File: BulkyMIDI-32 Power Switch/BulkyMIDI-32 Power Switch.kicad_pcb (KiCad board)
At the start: 2 copper layers, 100 x 100 mm, 57 parts, among them J1 DC IN, J2 CH2, J3 CH1, J4 CH3, J5 CH4, J6 Power Panel, J7 CH5, K1 HK19F-DC, K2 HK19F-DC, K3 HK19F-DC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

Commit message: Fixes panel errors and inconsistencies
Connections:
- D2 pad 1: GND -> PWR
- D2 pad 2: PWR -> +5V
- D3 pad 1: GND -> SYS
- D3 pad 2: SYS -> +5V
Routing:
- net +5V: track 204.6 -> 271.3 mm
- net PWR: track 37.6 -> 39.7 mm
- net SYS: track 47.2 -> 49.2 mm
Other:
- board text added: "BulkyMIDI-32 Power Switch (rev. B) github.com/tebl"
- board text removed: "BulkyMIDI-32 Power Switch (rev. A) github.com/tebl"

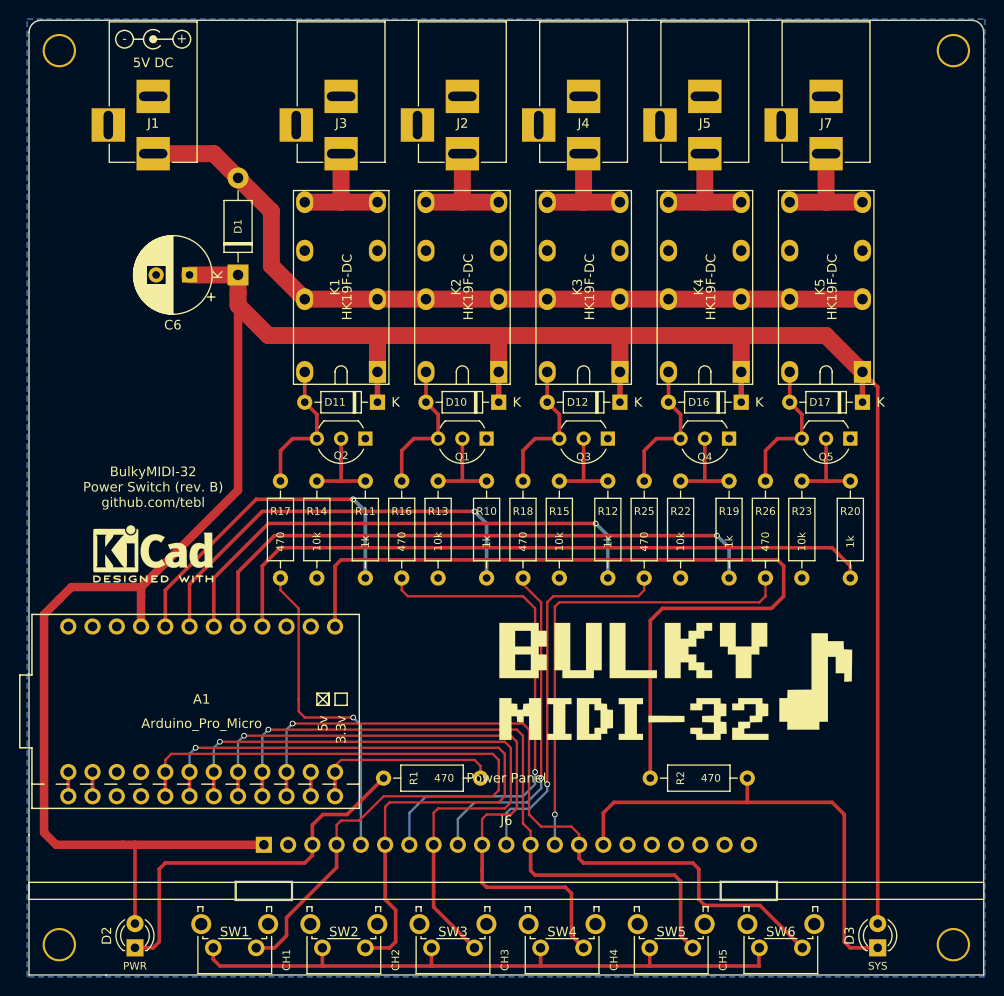
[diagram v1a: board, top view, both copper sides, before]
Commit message: Updated Power Switch to incorporate changes
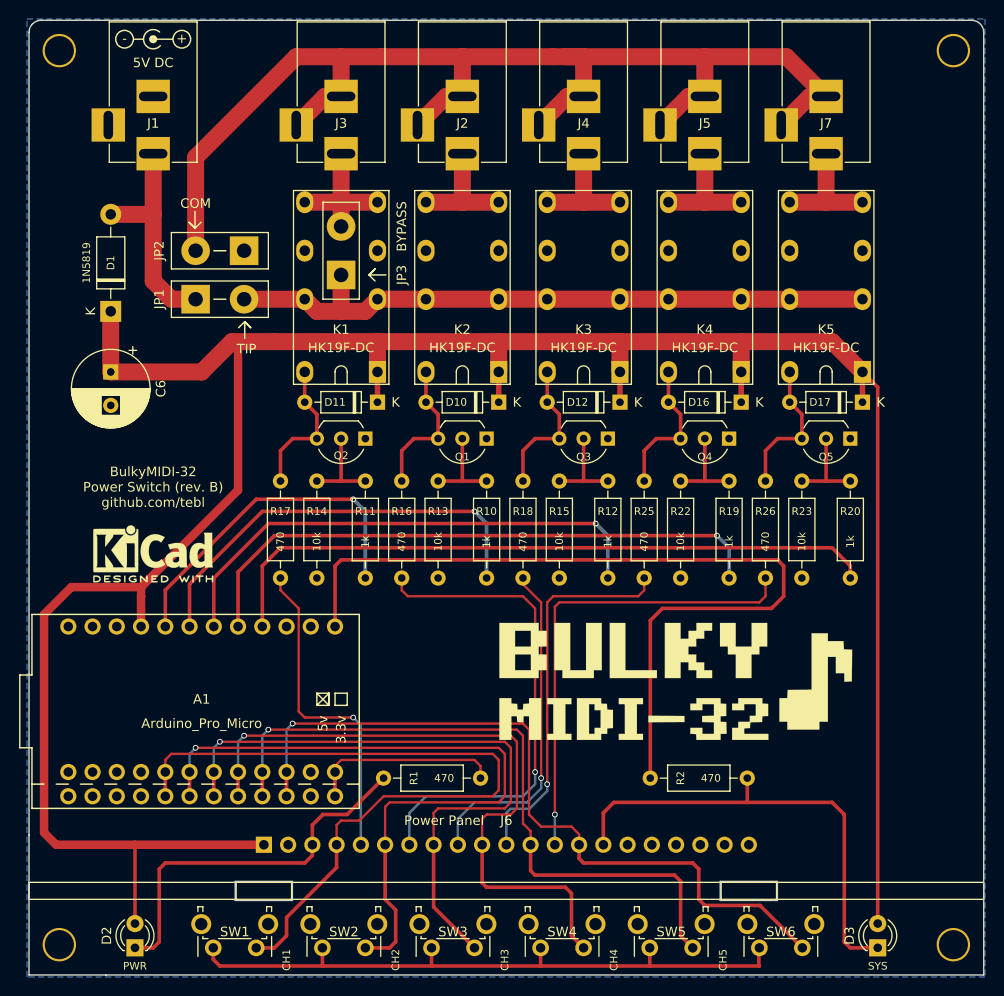
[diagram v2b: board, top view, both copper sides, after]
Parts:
- added JP1: TIP, wire_pads:WireLink, F.Cu at (87.6, 83.8)
- added JP2: COM, wire_pads:WireLink, F.Cu at (92.7, 78.7)
- added JP3: BYPASS, wire_pads:WireLink, F.Cu at (102.9, 81.3)
- moved D1 13.9 mm to (78.7, 85.1)
- moved C6 13.1 mm to (78.7, 91.4), turned to -90 degrees
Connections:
- A1 pad 1: Net-(A1-Pad1) -> unconnected-(A1-TXO-Pad1)_0
- A1 pad 11: Net-(A1-Pad11) -> unconnected-(A1-D8-Pad11)_0
- A1 pad 14: (no net) -> unconnected-(A1-D16-Pad14)
- A1 pad 15: (no net) -> unconnected-(A1-D14-Pad15)
- A1 pad 2: Net-(A1-Pad2) -> unconnected-(A1-RXI-Pad2)
- A1 pad 22: (no net) -> unconnected-(A1-RST-Pad22)
- A1 pad 24: (no net) -> unconnected-(A1-RAW-Pad24)
- J2 pad 2: GND -> DC_COM
- J2 pad 3: GND -> DC_COM
- J3 pad 2: GND -> DC_COM
- J3 pad 3: GND -> DC_COM
- J4 pad 2: GND -> DC_COM
- J4 pad 3: GND -> DC_COM
- J5 pad 2: GND -> DC_COM
- J5 pad 3: GND -> DC_COM
- J6 pad 16: (no net) -> unconnected-(J6-N.C.-Pad16)
- J6 pad 17: (no net) -> unconnected-(J6-N.C.-Pad17)
- J6 pad 18: (no net) -> unconnected-(J6-N.C.-Pad18)
- J6 pad 19: (no net) -> unconnected-(J6-N.C.-Pad19)
- J6 pad 21: (no net) -> unconnected-(J6-N.C.-Pad21)
- J7 pad 2: GND -> DC_COM
- J7 pad 3: GND -> DC_COM
- K1 pad 11: (no net) -> unconnected-(K1-NC_2-Pad11)
- K1 pad 13: VIN -> DC_TIP
- K1 pad 4: VIN -> DC_TIP
- K1 pad 6: (no net) -> unconnected-(K1-NC_1-Pad6)
- K2 pad 11: (no net) -> unconnected-(K2-NC_2-Pad11)
- K2 pad 13: VIN -> DC_TIP
- K2 pad 4: VIN -> DC_TIP
- K2 pad 6: (no net) -> unconnected-(K2-NC_1-Pad6)
- K3 pad 11: (no net) -> unconnected-(K3-NC_2-Pad11)
- K3 pad 13: VIN -> DC_TIP
- K3 pad 4: VIN -> DC_TIP
- K3 pad 6: (no net) -> unconnected-(K3-NC_1-Pad6)
- K4 pad 11: (no net) -> unconnected-(K4-NC_2-Pad11)
- K4 pad 13: VIN -> DC_TIP
- K4 pad 4: VIN -> DC_TIP
- K4 pad 6: (no net) -> unconnected-(K4-NC_1-Pad6)
- K5 pad 11: (no net) -> unconnected-(K5-NC_2-Pad11)
- K5 pad 13: VIN -> DC_TIP
- K5 pad 4: VIN -> DC_TIP
- K5 pad 6: (no net) -> unconnected-(K5-NC_1-Pad6)
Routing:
- net DC_COM: track 0.00 -> 130.1 mm
- net DC_TIP: track 0.00 -> 69.6 mm
- net VIN: track 84.0 -> 23.0 mm
- net +5V: track 271.3 -> 279.2 mm
- net Net-(JP3-B): track 12.7 -> 15.2 mm
- net Net-(A1-Pad2): track 2.54 -> 0.00 mm
- net Net-(A1-Pad11): track 2.54 -> 0.00 mm
- net Net-(A1-Pad1): track 2.54 -> 0.00 mm
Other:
- net class Default removed
- net class Power removed
- net class Power2 removed

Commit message: Updated Power Switch
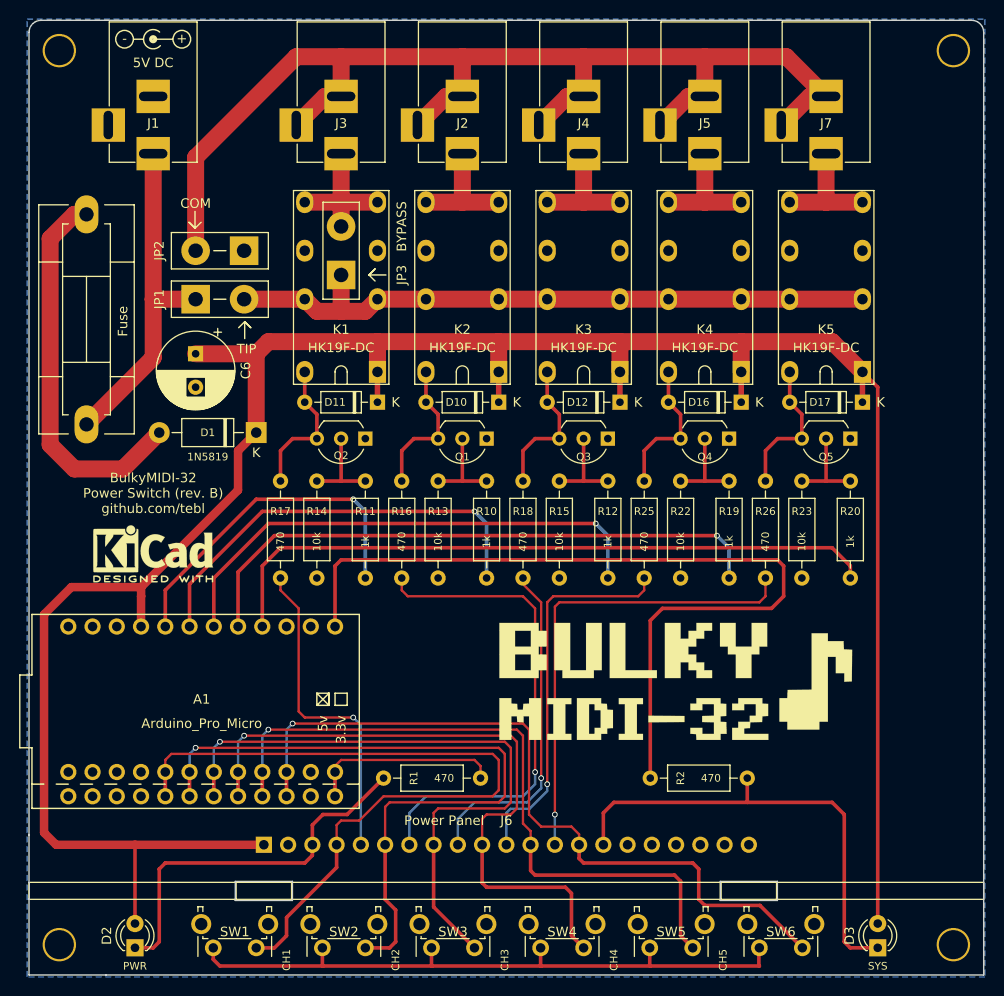
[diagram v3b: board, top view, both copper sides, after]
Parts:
- added F1: Fuse, BulkyMIDI-32:Fuseholder5x20_horiz_SemiClosed_Casing10x25mm, F.Cu at (76.2, 96.9)
- M1, M2, M3, M4: footprint mounting:M3 -> mounting:M3_pin
- moved D1 19.8 mm to (94.0, 97.8), turned to 180 degrees
- moved C6 9.09 mm to (87.6, 89.5)
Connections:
- D1 pad 2: VIN -> Net-(D1-A)
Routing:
- net Net-(D1-A): track 0.00 -> 40.5 mm
- net +5V: track 279.2 -> 258.9 mm
- net VIN: track 23.0 -> 35.7 mm
- net DC_COM: track 130.1 -> 128.2 mm
- net /LED3: track 35.6 -> 34.9 mm
- net Net-(A1-D9): track 20.2 -> 19.6 mm
